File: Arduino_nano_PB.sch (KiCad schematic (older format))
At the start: 42 parts, among them CON1 BARREL_JACK, P1 CONN_01X02, P7 CONN_01X04, Q1 BC547, Q2 BC547, Q3 BC547, Q4 Q_NPN_EBC, Q5 Q_NPN_EBC, Q6 Q_NPN_EBC, Q7 Q_NPN_EBC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

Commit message: añadir valores en esquema y reordenar PCB
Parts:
- C1: footprint Capacitors_ThroughHole:C_Radial_D5_L11_P2.5 -> Capacitors_ThroughHole:C_Radial_D5_L11_P2; Fabricante (none) -> NICHICON; Provedor (none) -> TME; Ref (none) -> UMT1HR33MDD; Ref_Proveedor (none) -> UMT1HR33MDD
- C2: footprint Capacitors_ThroughHole:C_Radial_D5_L11_P2.5 -> Capacitors_ThroughHole:C_Radial_D5_L11_P2; Fabricante (none) -> NICHICON; Provedor (none) -> TME; Ref (none) -> UMT1H0R1MDD; Ref_Proveedor (none) -> UMT1H0R1MDD
- C3: value C -> 100n; footprint Capacitors_ThroughHole:C_Disc_D6_P5 -> Capacitors_ThroughHole:C_Disc_D3_P2.5
- D1: value D -> 1N4002; Fabricante (none) -> DC COMPONENTS; Provedor (none) -> TME; Ref (none) -> 1N4002; Ref_Proveedor (none) -> 1N4002-DC
- Led1: value Led_RGB_Anodo_Comun -> Led_RGB; Provedor tme -> TME
- P1, P7: Fabricante (none) -> TE CONNECTIVITY; Provedor (none) -> TME; Ref (none) -> 4-103321-8; Ref_Proveedor (none) -> 4-103321-8
- Q4, Q5, Q6, Q7, Q8: value Q_NPN_EBC -> 2N3904BU
- R1, R2, R3: value R -> 4K7
- R10, R12, R13, R14, R15, R8, R9: value R -> 120; Fabricante (none) -> SR_PASSIVES; Potencia (none) -> 1/4W; Provedor (none) -> TME; Ref (none) -> CF1/4W-120R; Ref_Proveedor (none) -> CF1/4W-120R; Tolerancia (none) -> 5%
- R11, R16, R17, R18, R19, R7: value R -> 1K; Fabricante (none) -> SR_PASSIVES; Potencia (none) -> 1/4W; Provedor (none) -> TME; Ref (none) -> CF1/4W-1K; Ref_Proveedor (none) -> CF1/4W-1K; Tolerancia (none) -> 5%
- R20: value Photores -> LDR; Fabricante (none) -> TOKEN; Provedor (none) -> TME; Ref (none) -> PGM5516; Ref_Proveedor (none) -> PGM5516
- R4, R5, R6: value R -> 100; Fabricante (none) -> SR PASSIVES; Potencia (none) -> 1/4W; Provedor (none) -> TME; Ref (none) -> CF1/4W-100R; Ref_Proveedor (none) -> CF1/4W-100R; Tolerancia (none) -> 5%
- RV1: value POT -> 10K; Fabricante (none) -> SR PASSIVES; Provedor (none) -> TME; Ref (none) -> R9011-1-10K; Ref_Proveedor (none) -> R9011-1-10K
- SP1: value SPEAKER -> BUZZER; Fabricante (none) -> LOUDITY; Provedor (none) -> TME; Ref (none) -> LD-BZPN-1705; Ref_Proveedor (none) -> LD-BZPN-1705
- U1: Fabricante (none) -> FAIRCHILD SEMICONDUCTOR; Provedor (none) -> TME; Ref (none) -> LM7805CT; Ref_Proveedor (none) -> LM7805CT
- U2: Fabricante (none) -> TEXAS INSTRUMENTS; Provedor (none) -> TME; Ref (none) -> SN74HC595D; Ref_Proveedor (none) -> SN74HC595D
- U3: value Matriz_5x7_Anodo_Filas -> Matriz_5x7; Fabricante (none) -> WENRUN; Provedor (none) -> TME; Ref (none) -> LMD07057BUE-101A; Ref_Proveedor (none) -> LMD07057BUE-101A
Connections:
- net +5V: now also R20.1; no longer R19.1
- net A0: now also R20.2; no longer R20.1
- net GND: now also R19.1; no longer R20.2
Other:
- note added: "ETAPA DE ALIMENTACION"
- note added: "I2C"
- note added: "PUERTO SERIE"
- note added: "PUERTOS DE EXPANSION"
- note added: "Rx"
- note added: "SCL"
- note added: "SDA"
- note added: "Tx"
- moved on the sheet: P1, P7, R20

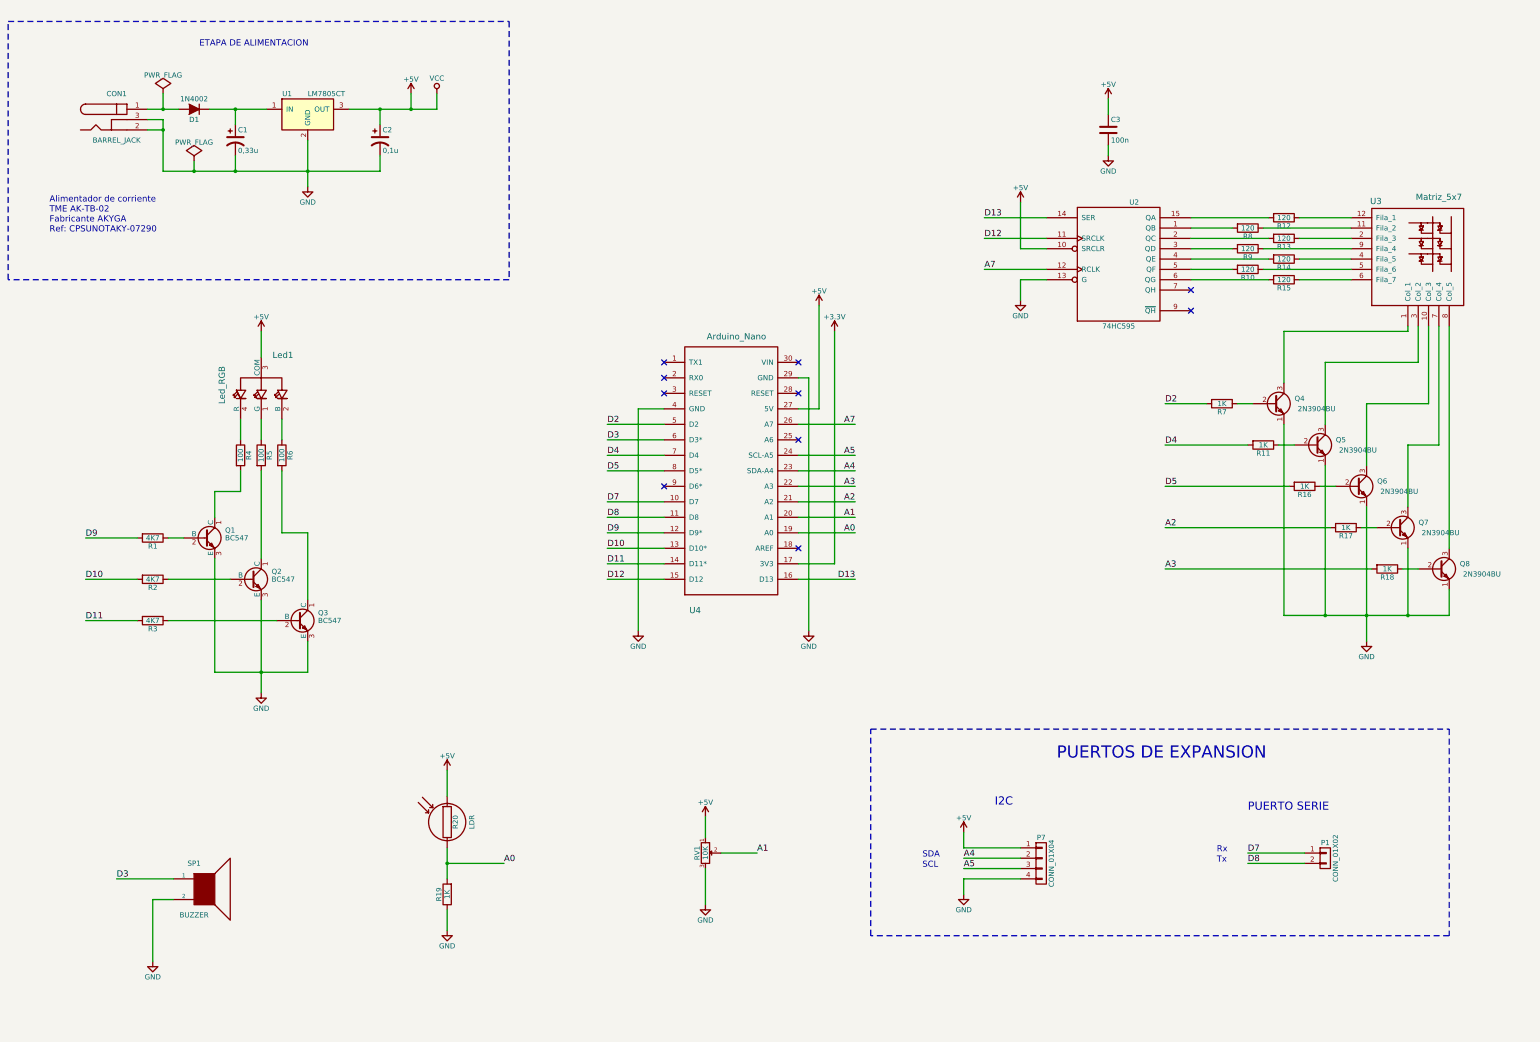
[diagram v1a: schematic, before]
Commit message: Añadir serigrafia capa bottom
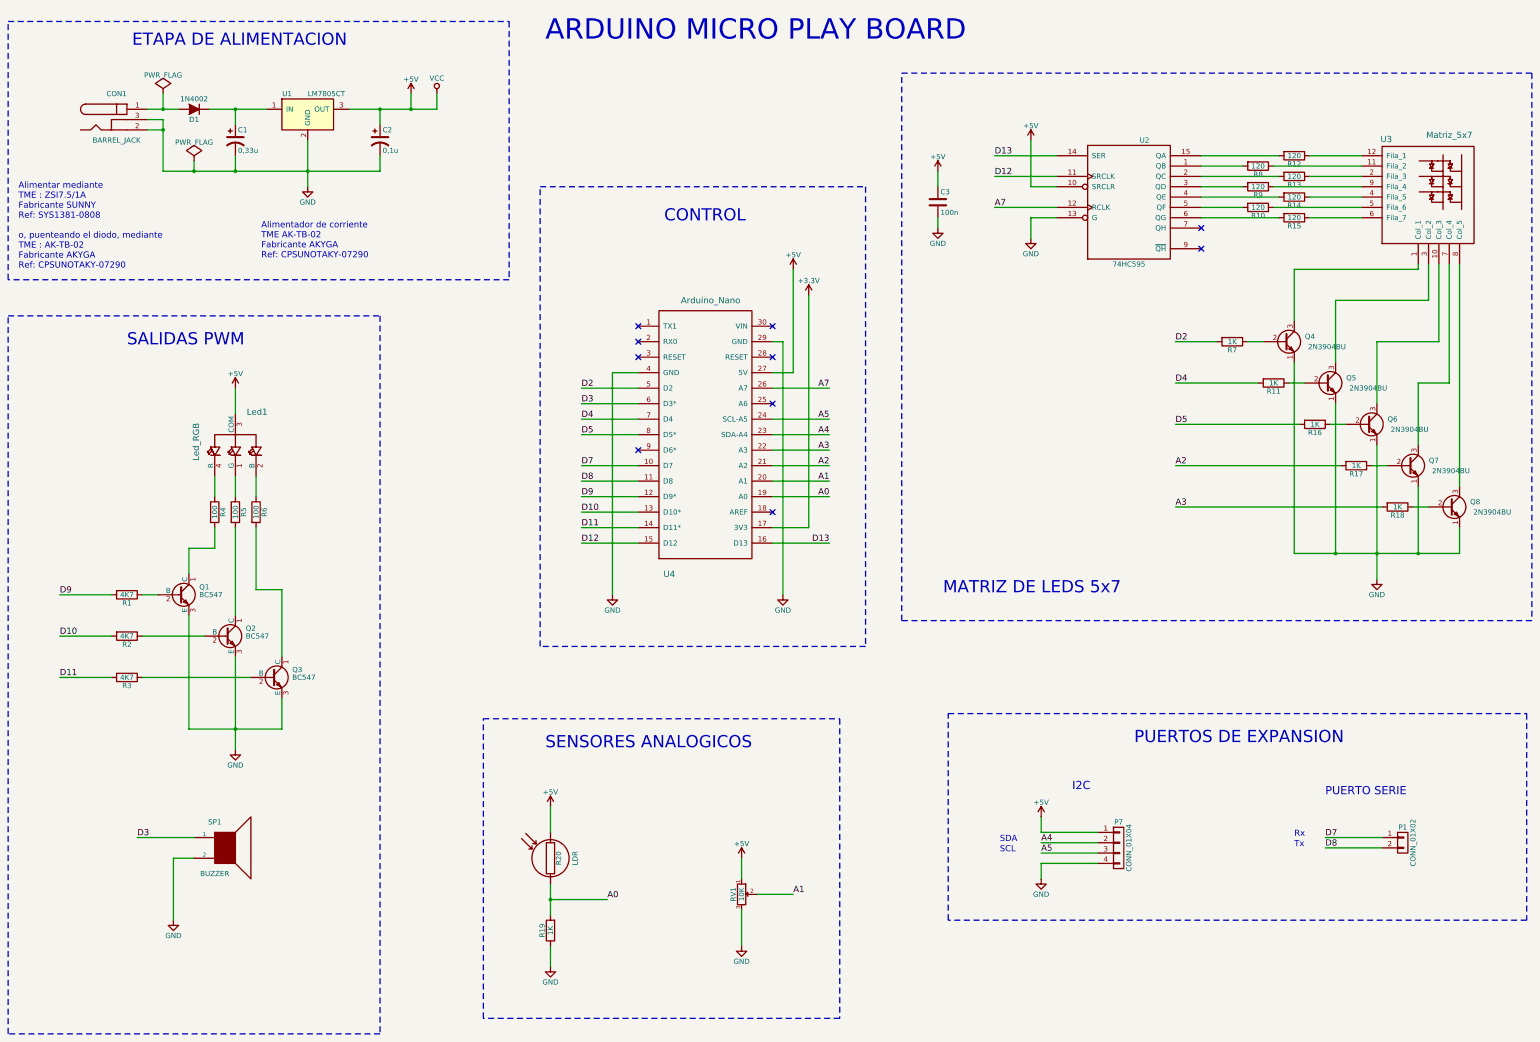
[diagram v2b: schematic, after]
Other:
- note added: "ARDUINO MICRO PLAY BOARD"
- note added: "Alimentar mediante\nTME : ZSI7.5/1A\nFabricante SUNNY\nRef: SYS1381-0808\n\no, puenteando el diodo, mediante\nTME : AK-TB-02\nFabricante AKYGA\nRef: CPSUNOTAKY-07290"
- note added: "CONTROL"
- note added: "MATRIZ DE LEDS 5x7"
- note added: "SALIDAS PWM"
- note added: "SENSORES ANALOGICOS"
- moved on the sheet: C3, Led1, P1, P7, Q1, Q2, Q3, Q4, Q5, Q6, Q7, Q8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

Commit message: modificar tamaños de taladros en led RGB y resistencias
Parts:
- Q1, Q2, Q3, Q4, Q5, Q6, Q7, Q8: footprint TO_SOT_Packages_THT:TO-92_Inline_Narrow_Oval -> Transistors:TO-92_EnLinea_Estrecho_Oval
- R1, R10, R11, R12, R13, R14, R15, R16, R17, R18, R19, R2, R3, R4, R5, R6, R7, R8, R9: footprint Resistors_ThroughHole:Resistor_Horizontal_RM10mm -> Resistencias:Resistencia_1_4_W_10_mm
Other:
- note added: "ARDUINO NANO PLAY BOARD"
- note removed: "ARDUINO MICRO PLAY BOARD"
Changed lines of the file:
@@
 F 0 "R4" V 2880 5550 50  0000 C CNN
 F 1 "100" V 2800 5550 50  0000 C CNN
-F 2 "Resistors_ThroughHole:Resistor_Horizontal_RM10mm" V 2730 5550 50  0001 C CNN
+F 2 "Resistencias:Resistencia_1_4_W_10_mm" V 2730 5550 50  0001 C CNN
 F 3 "" H 2800 5550 50  0000 C CNN
 F 4 "SR PASSIVES" H 2800 5550 60  0001 C CNN "Fabricante"
@@
 F 0 "Q1" H 2650 6425 50  0000 L CNN
 F 1 "BC547" H 2650 6350 50  0000 L CNN
-F 2 "TO_SOT_Packages_THT:TO-92_Inline_Narrow_Oval" H 2650 6275 50  0001 L CIN
+F 2 "Transistors:TO-92_EnLinea_Estrecho_Oval" H 2650 6275 50  0001 L CIN
 F 3 "" H 2450 6350 50  0000 L CNN
 F 4 "DIOTEC SEMICONDUCTOR" H 2450 6350 60  0001 C CNN "Fabricante"
@@
 F 0 "R1" V 2030 6350 50  0000 C CNN
 F 1 "4K7" V 1950 6350 50  0000 C CNN
-F 2 "Resistors_ThroughHole:Resistor_Horizontal_RM10mm" V 1880 6350 50  0001 C CNN
+F 2 "Resistencias:Resistencia_1_4_W_10_mm" V 1880 6350 50  0001 C CNN
 F 3 "" H 1950 6350 50  0000 C CNN
 F 4 "~" H 1950 6350 60  0001 C CNN "Fabricante"
@@
 F 0 "R2" V 2030 6750 50  0000 C CNN
 F 1 "4K7" V 1950 6750 50  0000 C CNN
-F 2 "Resistors_ThroughHole:Resistor_Horizontal_RM10mm" V 1880 6750 50  0001 C CNN
+F 2 "Resistencias:Resistencia_1_4_W_10_mm" V 1880 6750 50  0001 C CNN
 F 3 "" H 1950 6750 50  0000 C CNN
 	1    1950 6750
@@
 F 0 "R3" V 2030 7150 50  0000 C CNN
 F 1 "4K7" V 1950 7150 50  0000 C CNN
-F 2 "Resistors_ThroughHole:Resistor_Horizontal_RM10mm" V 1880 7150 50  0001 C CNN
+F 2 "Resistencias:Resistencia_1_4_W_10_mm" V 1880 7150 50  0001 C CNN
 F 3 "" H 1950 7150 50  0000 C CNN
 F 4 "~" H 1950 7150 60  0001 C CNN "Fabricante"
@@
 F 0 "Q2" H 3100 6825 50  0000 L CNN
 F 1 "BC547" H 3100 6750 50  0000 L CNN
-F 2 "TO_SOT_Packages_THT:TO-92_Inline_Narrow_Oval" H 3100 6675 50  0001 L CIN
+F 2 "Transistors:TO-92_EnLinea_Estrecho_Oval" H 3100 6675 50  0001 L CIN
 F 3 "" H 2900 6750 50  0000 L CNN
 F 4 "DIOTEC SEMICONDUCTOR" H 2900 6750 60  0001 C CNN "Fabricante"
@@
 F 0 "Q3" H 3550 7225 50  0000 L CNN
 F 1 "BC547" H 3550 7150 50  0000 L CNN
-F 2 "TO_SOT_Packages_THT:TO-92_Inline_Narrow_Oval" H 3550 7075 50  0001 L CIN
+F 2 "Transistors:TO-92_EnLinea_Estrecho_Oval" H 3550 7075 50  0001 L CIN
 F 3 "" H 3350 7150 50  0000 L CNN
 F 4 "DIOTEC SEMICONDUCTOR" H 3350 7150 60  0001 C CNN "Fabricante"
@@
 F 0 "R12" V 13330 2100 50  0000 C CNN
 F 1 "120" V 13250 2100 50  0000 C CNN
-F 2 "Resistors_ThroughHole:Resistor_Horizontal_RM10mm" V 13180 2100 50  0001 C CNN
+F 2 "Resistencias:Resistencia_1_4_W_10_mm" V 13180 2100 50  0001 C CNN
 F 3 "" H 13250 2100 50  0000 C CNN
 F 4 "SR_PASSIVES" H 13250 2100 60  0001 C CNN "Fabricante"
@@
 F 0 "Q4" H 13450 3950 50  0000 R CNN
 F 1 "2N3904BU" H 13750 3850 50  0000 R CNN
-F 2 "TO_SOT_Packages_THT:TO-92_Inline_Narrow_Oval" H 13350 4000 50  0001 C CNN
+F 2 "Transistors:TO-92_EnLinea_Estrecho_Oval" H 13350 4000 50  0001 C CNN
 F 3 "" H 13150 3900 50  0000 C CNN
 F 4 "FAIRCHILD SEMICONDUCTOR" H 13150 3900 60  0001 C CNN "Fabricante"
@@
 F 0 "Q5" H 13850 4350 50  0000 R CNN
 F 1 "2N3904BU" H 14150 4250 50  0000 R CNN
-F 2 "TO_SOT_Packages_THT:TO-92_Inline_Narrow_Oval" H 13750 4400 50  0001 C CNN
+F 2 "Transistors:TO-92_EnLinea_Estrecho_Oval" H 13750 4400 50  0001 C CNN
 F 3 "" H 13550 4300 50  0000 C CNN
 F 4 "FAIRCHILD SEMICONDUCTOR" H 13550 4300 60  0001 C CNN "Fabricante"
@@
 F 0 "Q6" H 14250 4750 50  0000 R CNN
 F 1 "2N3904BU" H 14550 4650 50  0000 R CNN
-F 2 "TO_SOT_Packages_THT:TO-92_Inline_Narrow_Oval" H 14150 4800 50  0001 C CNN
+F 2 "Transistors:TO-92_EnLinea_Estrecho_Oval" H 14150 4800 50  0001 C CNN
 F 3 "" H 13950 4700 50  0000 C CNN
 F 4 "FAIRCHILD SEMICONDUCTOR" H 13950 4700 60  0001 C CNN "Fabricante"
@@
 F 0 "Q7" H 14650 5150 50  0000 R CNN
 F 1 "2N3904BU" H 14950 5050 50  0000 R CNN
-F 2 "TO_SOT_Packages_THT:TO-92_Inline_Narrow_Oval" H 14550 5200 50  0001 C CNN
+F 2 "Transistors:TO-92_EnLinea_Estrecho_Oval" H 14550 5200 50  0001 C CNN
 F 3 "" H 14350 5100 50  0000 C CNN
 F 4 "FAIRCHILD SEMICONDUCTOR" H 14350 5100 60  0001 C CNN "Fabricante"
@@
 F 0 "Q8" H 15050 5550 50  0000 R CNN
 F 1 "2N3904BU" H 15350 5450 50  0000 R CNN
-F 2 "TO_SOT_Packages_THT:TO-92_Inline_Narrow_Oval" H 14950 5600 50  0001 C CNN
+F 2 "Transistors:TO-92_EnLinea_Estrecho_Oval" H 14950 5600 50  0001 C CNN
 F 3 "" H 14750 5500 50  0000 C CNN
 F 4 "FAIRCHILD SEMICONDUCTOR" H 14750 5500 60  0001 C CNN "Fabricante"
@@
 F 0 "R8" V 12980 2200 50  0000 C CNN
 F 1 "120" V 12900 2200 50  0000 C CNN
-F 2 "Resistors_ThroughHole:Resistor_Horizontal_RM10mm" V 12830 2200 50  0001 C CNN
+F 2 "Resistencias:Resistencia_1_4_W_10_mm" V 12830 2200 50  0001 C CNN
 F 3 "" H 12900 2200 50  0000 C CNN
 F 4 "SR_PASSIVES" H 12900 2200 60  0001 C CNN "Fabricante"
@@
 F 0 "R9" V 12980 2400 50  0000 C CNN
 F 1 "120" V 12900 2400 50  0000 C CNN
-F 2 "Resistors_ThroughHole:Resistor_Horizontal_RM10mm" V 12830 2400 50  0001 C CNN
+F 2 "Resistencias:Resistencia_1_4_W_10_mm" V 12830 2400 50  0001 C CNN
 F 3 "" H 12900 2400 50  0000 C CNN
 F 4 "SR_PASSIVES" H 12900 2400 60  0001 C CNN "Fabricante"
@@
 F 0 "R10" V 12980 2600 50  0000 C CNN
 F 1 "120" V 12900 2600 50  0000 C CNN
-F 2 "Resistors_ThroughHole:Resistor_Horizontal_RM10mm" V 12830 2600 50  0001 C CNN
+F 2 "Resistencias:Resistencia_1_4_W_10_mm" V 12830 2600 50  0001 C CNN
 F 3 "" H 12900 2600 50  0000 C CNN
 F 4 "SR_PASSIVES" H 12900 2600 60  0001 C CNN "Fabricante"
@@
 F 0 "R13" V 13330 2300 50  0000 C CNN
 F 1 "120" V 13250 2300 50  0000 C CNN
-F 2 "Resistors_ThroughHole:Resistor_Horizontal_RM10mm" V 13180 2300 50  0001 C CNN
+F 2 "Resistencias:Resistencia_1_4_W_10_mm" V 13180 2300 50  0001 C CNN
 F 3 "" H 13250 2300 50  0000 C CNN
 F 4 "SR_PASSIVES" H 13250 2300 60  0001 C CNN "Fabricante"
@@
 F 0 "R14" V 13330 2500 50  0000 C CNN
 F 1 "120" V 13250 2500 50  0000 C CNN
-F 2 "Resistors_ThroughHole:Resistor_Horizontal_RM10mm" V 13180 2500 50  0001 C CNN
+F 2 "Resistencias:Resistencia_1_4_W_10_mm" V 13180 2500 50  0001 C CNN
 F 3 "" H 13250 2500 50  0000 C CNN
 F 4 "SR_PASSIVES" H 13250 2500 60  0001 C CNN "Fabricante"
@@
 F 0 "R15" V 13330 2700 50  0000 C CNN
 F 1 "120" V 13250 2700 50  0000 C CNN
-F 2 "Resistors_ThroughHole:Resistor_Horizontal_RM10mm" V 13180 2700 50  0001 C CNN
+F 2 "Resistencias:Resistencia_1_4_W_10_mm" V 13180 2700 50  0001 C CNN
 F 3 "" H 13250 2700 50  0000 C CNN
 F 4 "SR_PASSIVES" H 13250 2700 60  0001 C CNN "Fabricante"
@@
 F 0 "R7" V 12730 3900 50  0000 C CNN
 F 1 "1K" V 12650 3900 50  0000 C CNN
-F 2 "Resistors_ThroughHole:Resistor_Horizontal_RM10mm" V 12580 3900 50  0001 C CNN
+F 2 "Resistencias:Resistencia_1_4_W_10_mm" V 12580 3900 50  0001 C CNN
 F 3 "" H 12650 3900 50  0000 C CNN
 F 4 "SR_PASSIVES" H 12650 3900 60  0001 C CNN "Fabricante"
@@
 F 0 "R11" V 13130 4300 50  0000 C CNN
 F 1 "1K" V 13050 4300 50  0000 C CNN
-F 2 "Resistors_ThroughHole:Resistor_Horizontal_RM10mm" V 12980 4300 50  0001 C CNN
+F 2 "Resistencias:Resistencia_1_4_W_10_mm" V 12980 4300 50  0001 C CNN
 F 3 "" H 13050 4300 50  0000 C CNN
 F 4 "SR_PASSIVES" H 13050 4300 60  0001 C CNN "Fabricante"
@@
 F 0 "R16" V 13530 4700 50  0000 C CNN
 F 1 "1K" V 13450 4700 50  0000 C CNN
-F 2 "Resistors_ThroughHole:Resistor_Horizontal_RM10mm" V 13380 4700 50  0001 C CNN
+F 2 "Resistencias:Resistencia_1_4_W_10_mm" V 13380 4700 50  0001 C CNN
 F 3 "" H 13450 4700 50  0000 C CNN
 F 4 "SR_PASSIVES" H 13450 4700 60  0001 C CNN "Fabricante"
@@
 F 0 "R17" V 13930 5100 50  0000 C CNN
 F 1 "1K" V 13850 5100 50  0000 C CNN
-F 2 "Resistors_ThroughHole:Resistor_Horizontal_RM10mm" V 13780 5100 50  0001 C CNN
+F 2 "Resistencias:Resistencia_1_4_W_10_mm" V 13780 5100 50  0001 C CNN
 F 3 "" H 13850 5100 50  0000 C CNN
 F 4 "SR_PASSIVES" H 13850 5100 60  0001 C CNN "Fabricante"
@@
 F 0 "R18" V 14330 5500 50  0000 C CNN
 F 1 "1K" V 14250 5500 50  0000 C CNN
-F 2 "Resistors_ThroughHole:Resistor_Horizontal_RM10mm" V 14180 5500 50  0001 C CNN
+F 2 "Resistencias:Resistencia_1_4_W_10_mm" V 14180 5500 50  0001 C CNN
 F 3 "" H 14250 5500 50  0000 C CNN
 F 4 "SR_PASSIVES" H 14250 5500 60  0001 C CNN "Fabricante"
@@
 F 0 "R5" V 3080 5550 50  0000 C CNN
 F 1 "100" V 3000 5550 50  0000 C CNN
-F 2 "Resistors_ThroughHole:Resistor_Horizontal_RM10mm" V 2930 5550 50  0001 C CNN
+F 2 "Resistencias:Resistencia_1_4_W_10_mm" V 2930 5550 50  0001 C CNN
 F 3 "" H 3000 5550 50  0000 C CNN
 F 4 "SR PASSIVES" H 3000 5550 60  0001 C CNN "Fabricante"
@@
 F 0 "R6" V 3280 5550 50  0000 C CNN
 F 1 "100" V 3200 5550 50  0000 C CNN
-F 2 "Resistors_ThroughHole:Resistor_Horizontal_RM10mm" V 3130 5550 50  0001 C CNN
+F 2 "Resistencias:Resistencia_1_4_W_10_mm" V 3130 5550 50  0001 C CNN
 F 3 "" H 3200 5550 50  0000 C CNN
 F 4 "SR PASSIVES" H 3200 5550 60  0001 C CNN "Fabricante"
@@
 F 0 "R19" V 6130 9600 50  0000 C CNN
 F 1 "1K" V 6050 9600 50  0000 C CNN
-F 2 "Resistors_ThroughHole:Resistor_Horizontal_RM10mm" V 5980 9600 50  0001 C CNN
+F 2 "Resistencias:Resistencia_1_4_W_10_mm" V 5980 9600 50  0001 C CNN
 F 3 "" H 6050 9600 50  0000 C CNN
 F 4 "SR_PASSIVES" H 6050 9600 60  0001 C CNN "Fabricante"
@@
 Alimentar mediante\nTME : ZSI7.5/1A\nFabricante SUNNY\nRef: SYS1381-0808\n\no, puenteando el diodo, mediante\nTME : AK-TB-02\nFabricante AKYGA\nRef: CPSUNOTAKY-07290
 Text Notes 6000 1000 0    197  ~ 0
-ARDUINO MICRO PLAY BOARD
+ARDUINO NANO PLAY BOARD
 $EndSCHEMATC

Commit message: corrige issue #2
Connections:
- net D6: now reaches U4.9 (D6*)
- net D6: now also U2.12 (RCLK)
- net A7: no longer names the net of U4.26 (A7)
- net A7: no longer U2.12 (RCLK)
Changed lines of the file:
@@
 LIBS:contrib
 LIBS:valves
+LIBS:MyLibrary
 LIBS:Arduino_nano_PB-cache
 EELAYER 25 0
@@
 Sheet 1 1
 Title ""
-Date "sam. 04 avril 2015"
-Rev ""
+Date "2016-07-18"
+Rev "a"
 Comp ""
 Comment1 ""
@@
 D12
 Text Label 10350 2600 0    60   ~ 0
-A7
+D6
 $Comp
 L Arduino_Nano U4
@@
 NoConn ~ 8200 4500
 Wire Wire Line
-	8200 4350 8750 4350
-Text Label 8750 4350 2    60   ~ 0
-A7
-Wire Wire Line
 	6900 4500 6350 4500
 Text Label 6350 4500 0    60   ~ 0
 D3
-NoConn ~ 6900 4950
 NoConn ~ 8200 3750
 $Comp
@@
 Text Notes 6000 1000 0    197  ~ 0
 ARDUINO NANO PLAY BOARD
+Wire Wire Line
+	6900 4950 6350 4950
+Text Label 6350 4950 0    60   ~ 0
+D6
+NoConn ~ 8200 4350
 $EndSCHEMATC
